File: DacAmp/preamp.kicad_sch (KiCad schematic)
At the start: 31 parts, among them U12 NE5532, U13 NE5532, U2 NE5532, U3 NE5532, U4 NE5532, U5 NE5532, U6 NE5532, U7 NE5532, U8 NE5532

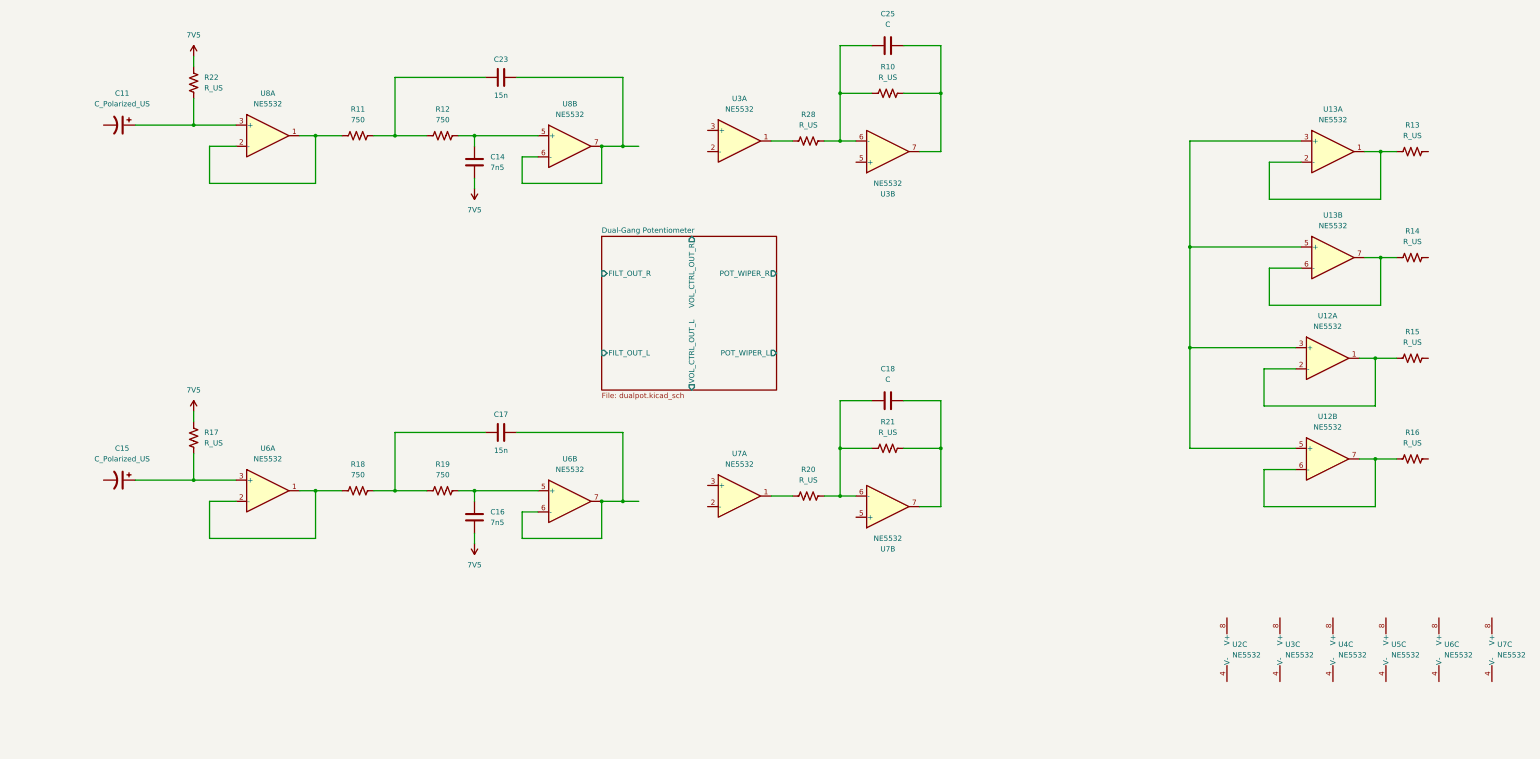
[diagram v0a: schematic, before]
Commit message: complete overall schematic, TODO: find values and add net labels
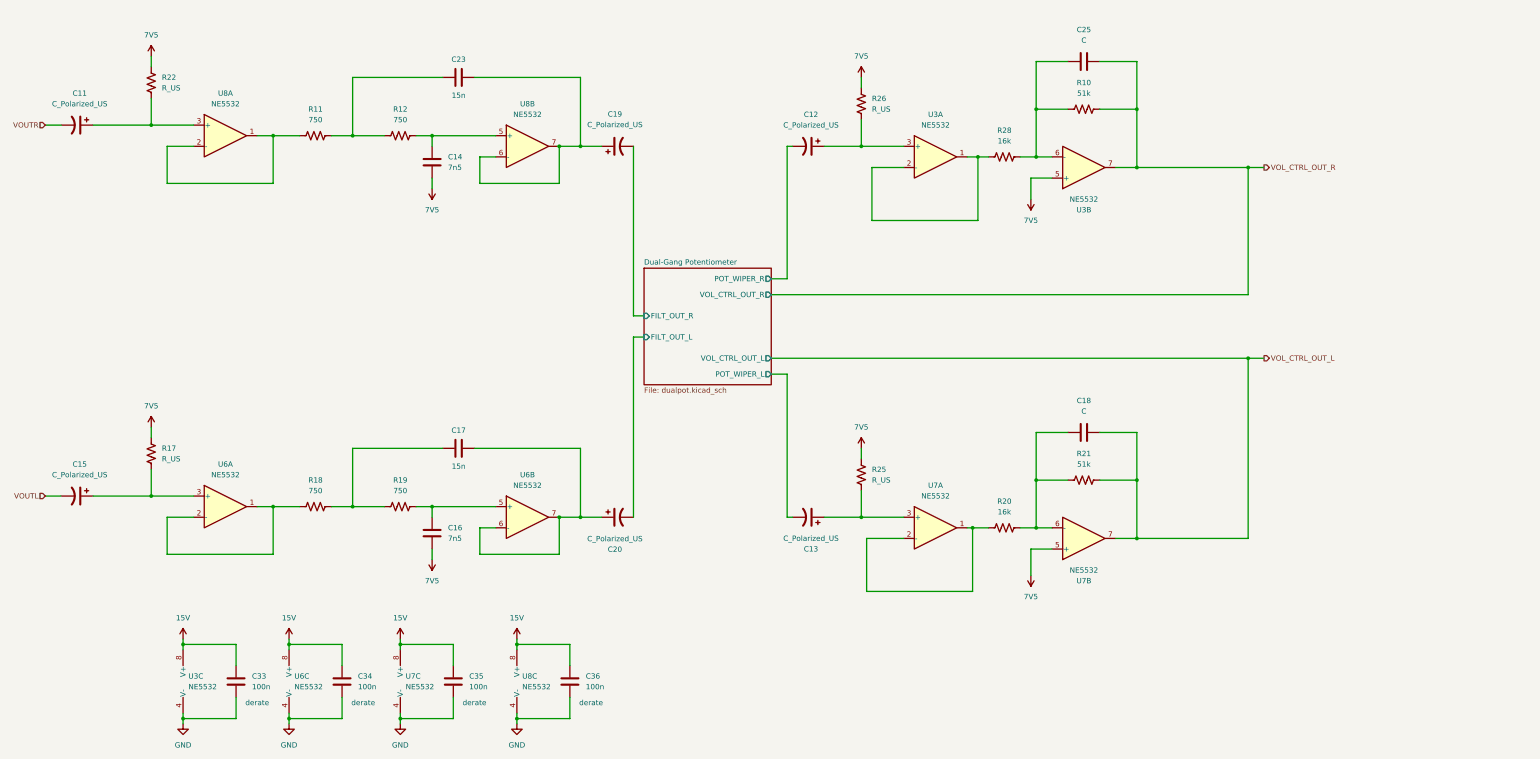
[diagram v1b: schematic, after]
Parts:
- removed R13, R14, R15, R16: R_US, symbol Device:R_US
- removed U12, U13, U2, U4, U5: NE5532, symbol Amplifier_Operational:NE5532
- added C12, C13, C19, C20: C_Polarized_US, symbol Device:C_Polarized_US
- added C33, C34, C35, C36: 100n, symbol Device:C
- added R25, R26: R_US, symbol Device:R_US
- added unit 3 of U8
- R10, R21: value R_US -> 51k
- R20, R28: value R_US -> 16k
- U3, U6, U7, U8: footprint (none) -> Package_SO:SOIC-8_3.9x4.9mm_P1.27mm
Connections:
- net 7V5: now also U3.5 (+), U7.5 (+), R25.1, R26.1
- net Dual-Gang Potentiometer/FILT_OUT_L: now also C20.2
- net Dual-Gang Potentiometer/FILT_OUT_R: now also C19.2
- net Dual-Gang Potentiometer/POT_WIPER_L: now also C13.2
- net Dual-Gang Potentiometer/POT_WIPER_R: now also C12.2
- net VOL_CTRL_OUT_L: now reaches C18.2, R21.2, U7.7
- net at R28.1, U3.1: now also U3.2 (-)
- net at U3.3 (+): now also C12.1, R26.2
- net GND: now reaches U7.4 (V-)
- net GND: now also U3.4 (V-), U6.4 (V-), C33.2, C34.2, C35.2, C36.2, U8.4 (V-)
- net 15V: now reaches U7.8 (V+)
- net 15V: now also U3.8 (V+), U6.8 (V+), C33.1, C34.1, C35.1, C36.1, U8.8 (V+)
- net at C23.2, U8.6 (-), U8.7: now also C19.1
- net VOL_CTRL_OUT_R: now reaches C25.2, R10.2, U3.7
- net VOUTR: now reaches C11.2
- net at R20.1, U7.1: now also U7.2 (-)
- net VOUTL: now reaches C15.2
- net at C17.2, U6.6 (-), U6.7: now also C20.1
- net at U7.3 (+): now also C13.1, R25.2
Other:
- note added: "derate"
- moved on the sheet: C11, C14, C15, C16, C17, C18, C23, C25, R10, R11, R12, R17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

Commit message: add 15v LDO
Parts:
- C33, C34, C35, C36: footprint (none) -> Capacitor_SMD:C_0805_2012Metric_Pad1.18x1.45mm_HandSolder

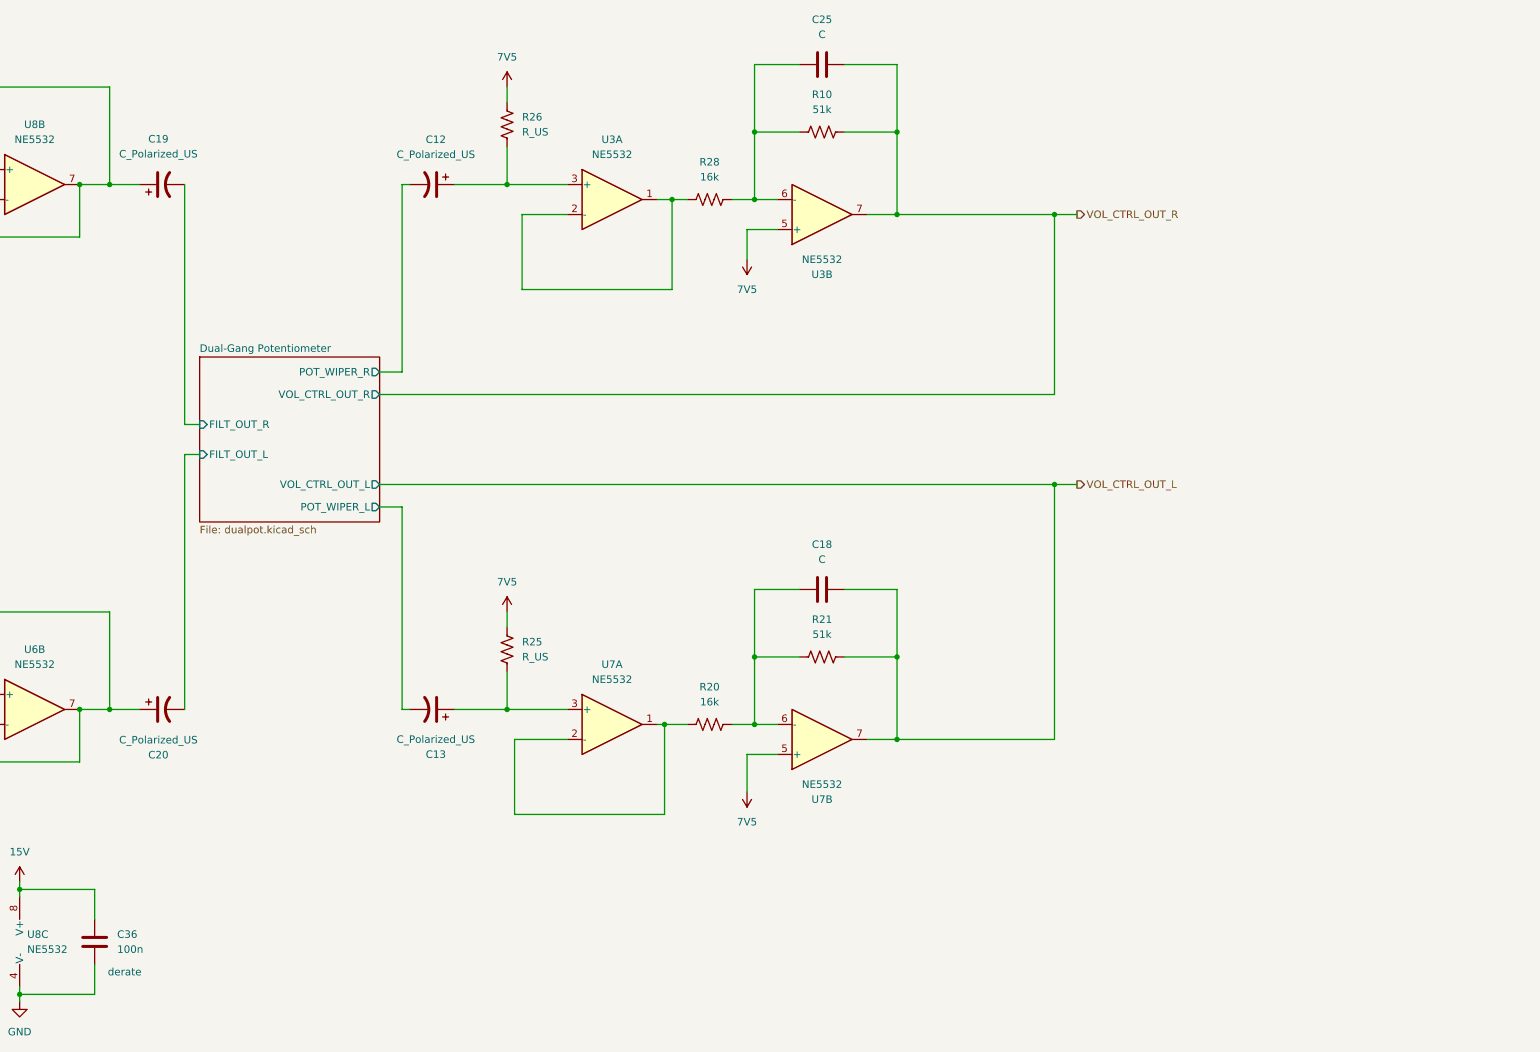
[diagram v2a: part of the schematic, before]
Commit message: added phase reversal to volume control stage
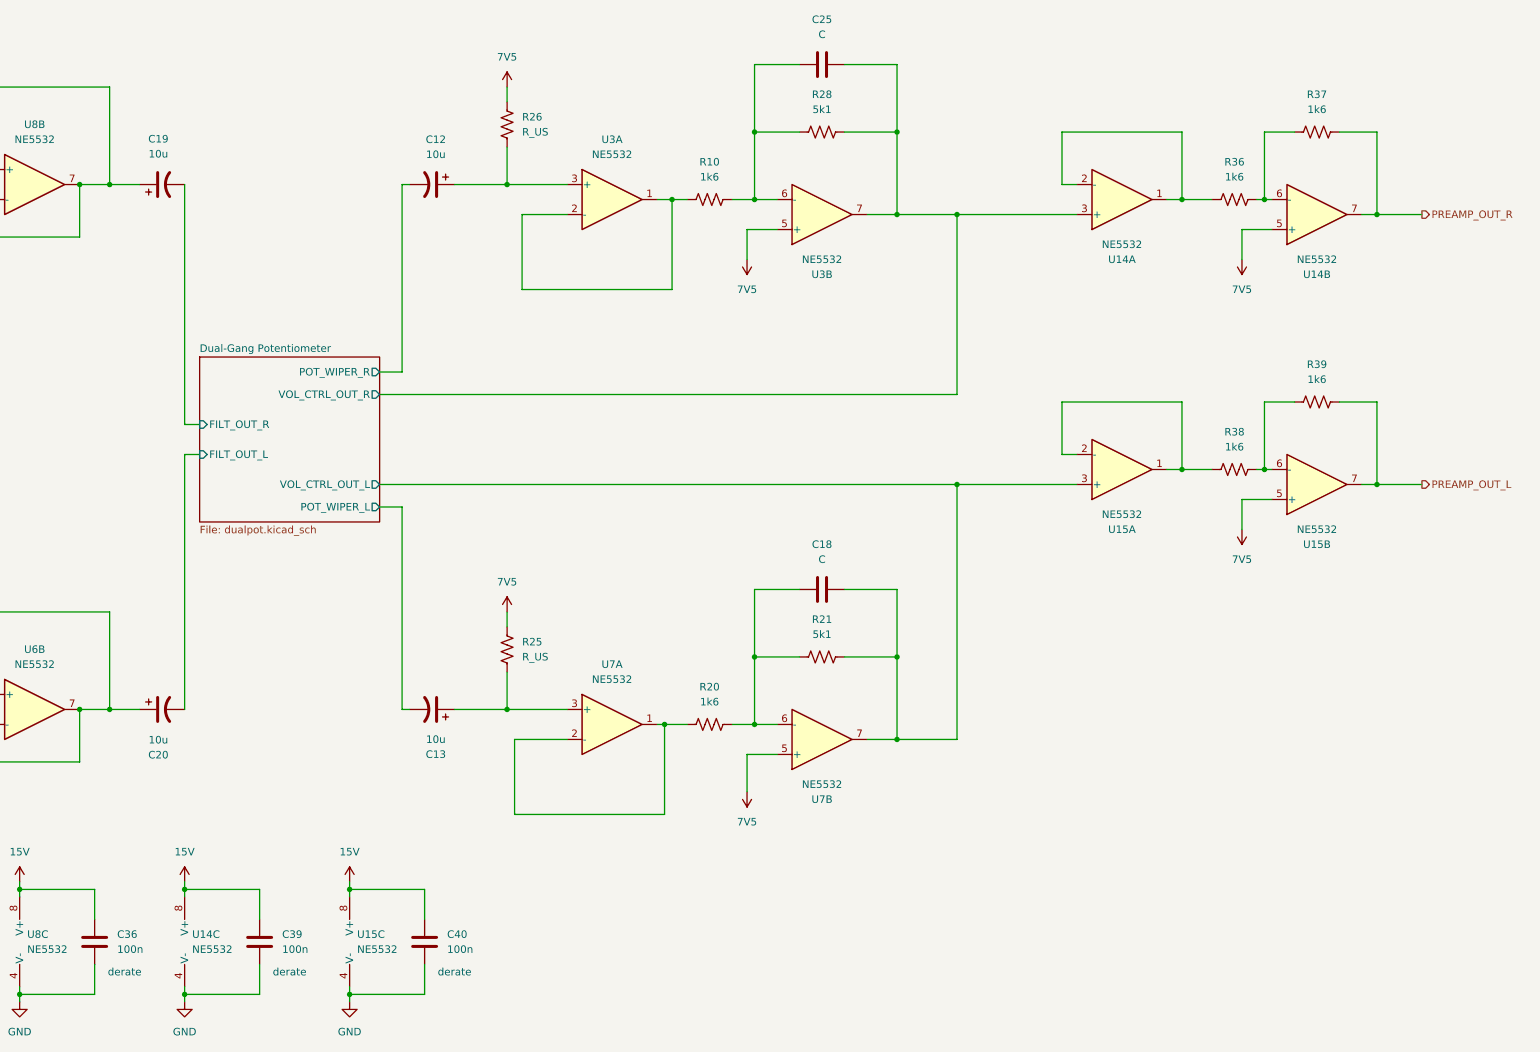
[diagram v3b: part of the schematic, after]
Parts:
- added C39, C40: 100n, Capacitor_SMD:C_0805_2012Metric_Pad1.18x1.45mm_HandSolder, symbol Device:C
- added R36, R37, R38, R39: 1k6, symbol Device:R_US
- added U14, U15: NE5532, symbol Amplifier_Operational:NE5532
- C12, C13, C19, C20: value C_Polarized_US -> 10u
- R10: value 51k -> 1k6
- R20: value 16k -> 1k6
- R21: value 51k -> 5k1
- R28: value 16k -> 5k1
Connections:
- net 15V: now also C39.1, C40.1, U14.8 (V+), U15.8 (V+)
- net 7V5: now also U14.5 (+), U15.5 (+)
- net GND: now also C39.2, C40.2, U14.4 (V-), U15.4 (V-)
- net at U3.1, U3.2 (-): now also R10.1; no longer R28.1
- net at C25.1, U3.6 (-): now also R10.2, R28.1; no longer R10.1, R28.2
- net VOL_CTRL_OUT_L renamed Dual-Gang Potentiometer/VOL_CTRL_OUT_L
- net Dual-Gang Potentiometer/VOL_CTRL_OUT_L: now also U15.3 (+)
- net VOL_CTRL_OUT_R renamed Dual-Gang Potentiometer/VOL_CTRL_OUT_R
- net Dual-Gang Potentiometer/VOL_CTRL_OUT_R: now also R28.2, U14.3 (+); no longer R10.2
- new net: R38.1, U15.1, U15.2 (-)
- new net: R38.2, R39.1, U15.6 (-)
- new net: R36.1, U14.1, U14.2 (-)
- new net: R36.2, R37.1, U14.6 (-)
- new net PREAMP_OUT_L: R39.2, U15.7
- new net PREAMP_OUT_R: R37.2, U14.7

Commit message: make preamp diagram block-y
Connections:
- net VOL_OUT_BUF_L: now reaches R38.1, U15.1, U15.2 (-)
- net VOL_OUT_BUF_R: now reaches R36.1, U14.1, U14.2 (-)
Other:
- note added: "-3dB @ 20kHz"
- note added: "Baxandall Volume Control (Inverting)"
- note added: "Input Buffer & Virtual Zeroing"
- note added: "Re-Inversion (phase recovery)"
- note added: "Sallen-Key Low Pass Filter"
- moved on the sheet: C11, C12, C13, C14, C15, C16, C17, C18, C19, C20, C23, C25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

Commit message: removed redundant inversion, applied inversion to input buffers
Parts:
- removed C39, C40: 100n, Capacitor_SMD:C_0805_2012Metric_Pad1.18x1.45mm_HandSolder, symbol Device:C
- removed R36, R37, R38, R39: 1k6, symbol Device:R_US
- removed U14, U15: NE5532, symbol Amplifier_Operational:NE5532
- added R40, R41: 20k, symbol Device:R_US
- C11, C15: value C_Polarized_US -> 10u
- R17, R22, R25, R26: value R_US -> 20k
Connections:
- net Dual-Gang Potentiometer/VOL_CTRL_OUT_L is gone; now on net PREAMP_OUT_L: C18.2, R21.2, U7.7
- net Dual-Gang Potentiometer/VOL_CTRL_OUT_R is gone; now on net PREAMP_OUT_R: C25.2, R28.2, U3.7
- net 7V5: now also U6.3 (+), U8.3 (+); no longer R17.1, R22.1
- net FILT_IN_L: now reaches R18.1, U6.1
- net FILT_IN_L: now also R41.2; no longer U6.2 (-)
- net VC_BUF_R: now reaches R10.1, U3.1, U3.2 (-)
- net VC_INR: now reaches C12.1, R26.2, U3.3 (+)
- net FILT_R: now reaches C19.1, C23.2, U8.6 (-), U8.7
- net VC_INL: now reaches C13.1, R25.2, U7.3 (+)
- net VC_BUF_L: now reaches R20.1, U7.1, U7.2 (-)
- net FILT_L: now reaches C17.2, C20.1, U6.6 (-), U6.7
- net FILT_IN_R: now reaches R11.1, U8.1
- net FILT_IN_R: now also R40.2; no longer U8.2 (-)
- new net: R17.2, R41.1, U6.2 (-)
- new net: R22.2, R40.1, U8.2 (-)
- new net PREAMP_INL: C15.1, R17.1
- new net PREAMP_INR: C11.1, R22.1
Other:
- note added: "Inverting buffer Offset shifting"
- note removed: "Input Buffer & Virtual Zeroing"
- note removed: "Re-Inversion (phase recovery)"
- moved on the sheet: U8A

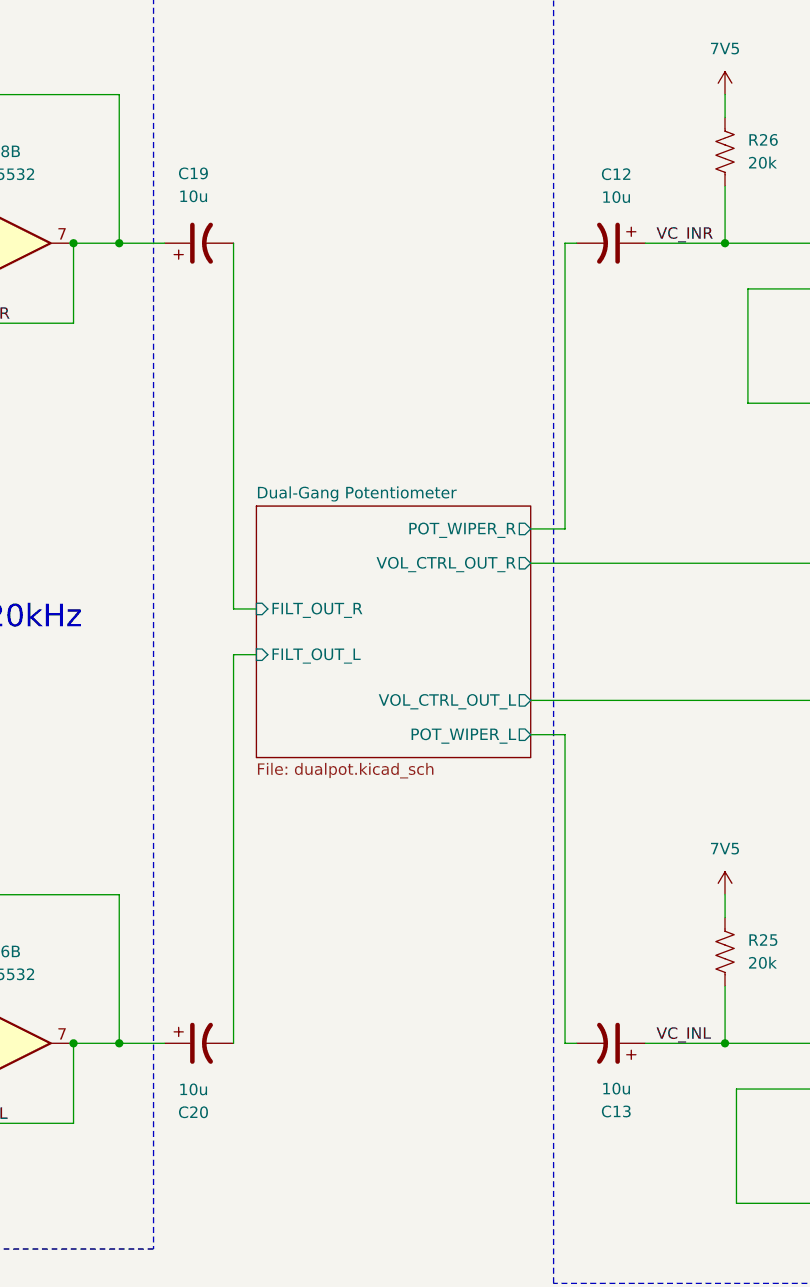
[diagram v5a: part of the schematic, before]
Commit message: add footprints to almost everything
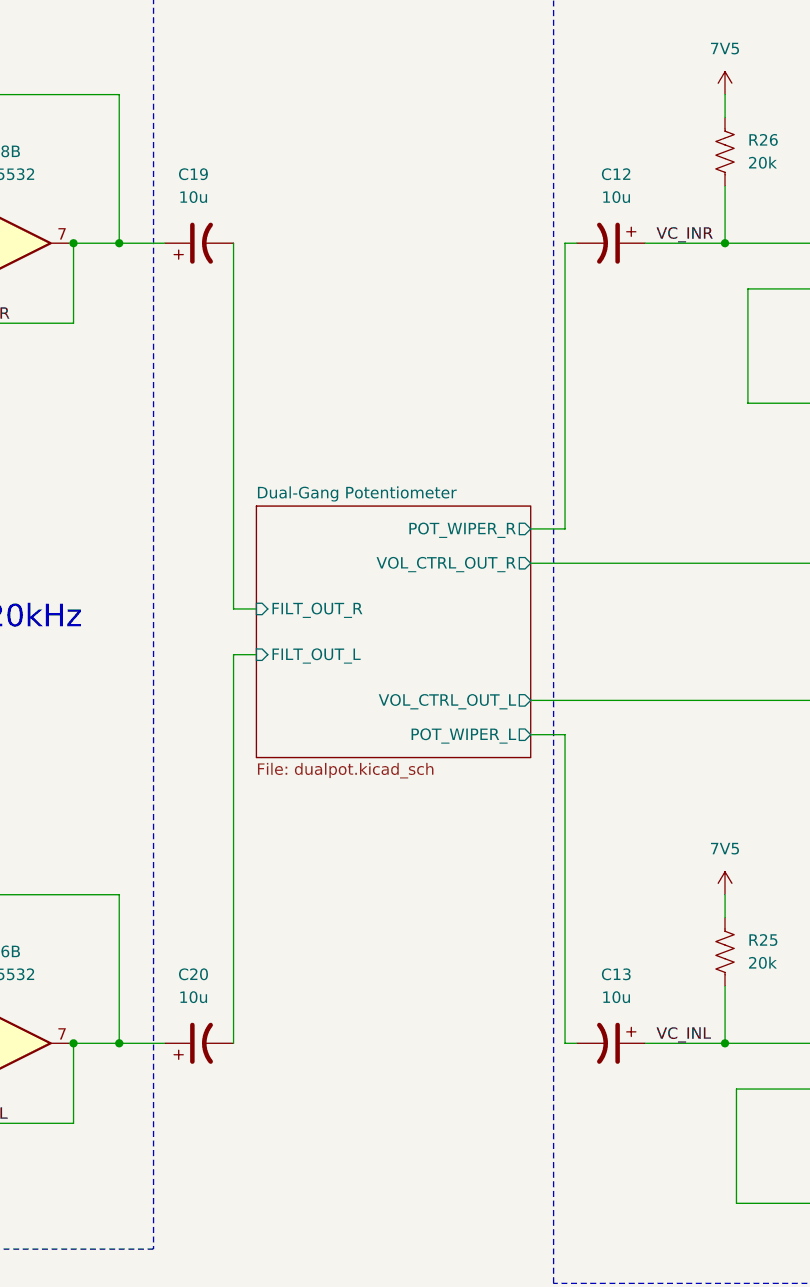
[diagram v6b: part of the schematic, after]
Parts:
- C11, C12, C13, C15, C19, C20: footprint (none) -> Capacitor_THT:CP_Radial_D5.0mm_P2.00mm
- C14, C16: footprint (none) -> Capacitor_SMD:C_0603_1608Metric_Pad1.08x0.95mm_HandSolder
- C17, C23: footprint (none) -> Capacitor_SMD:C_0805_2012Metric_Pad1.18x1.45mm_HandSolder
- R10, R11, R12, R17, R18, R19, R20, R21, R22, R25, R26, R28, R40, R41: footprint (none) -> Resistor_SMD:R_0402_1005Metric_Pad0.72x0.64mm_HandSolder
